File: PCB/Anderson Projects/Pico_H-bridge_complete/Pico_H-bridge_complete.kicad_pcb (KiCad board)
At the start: 2 copper layers, 120.2 x 65.5 mm, 92 parts, among them J1 Screw_Terminal_01x10, J2 Motor Connector, Q1 AO3400A, Q2 AO3400A, Q3 DMP3130LQ-7, Q4 DMP3130LQ-7, SW1 SW_DIP_x01, U1 Pico, U10 SN74LVC1G14DBV, U11 SN74LVC1G14DBV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

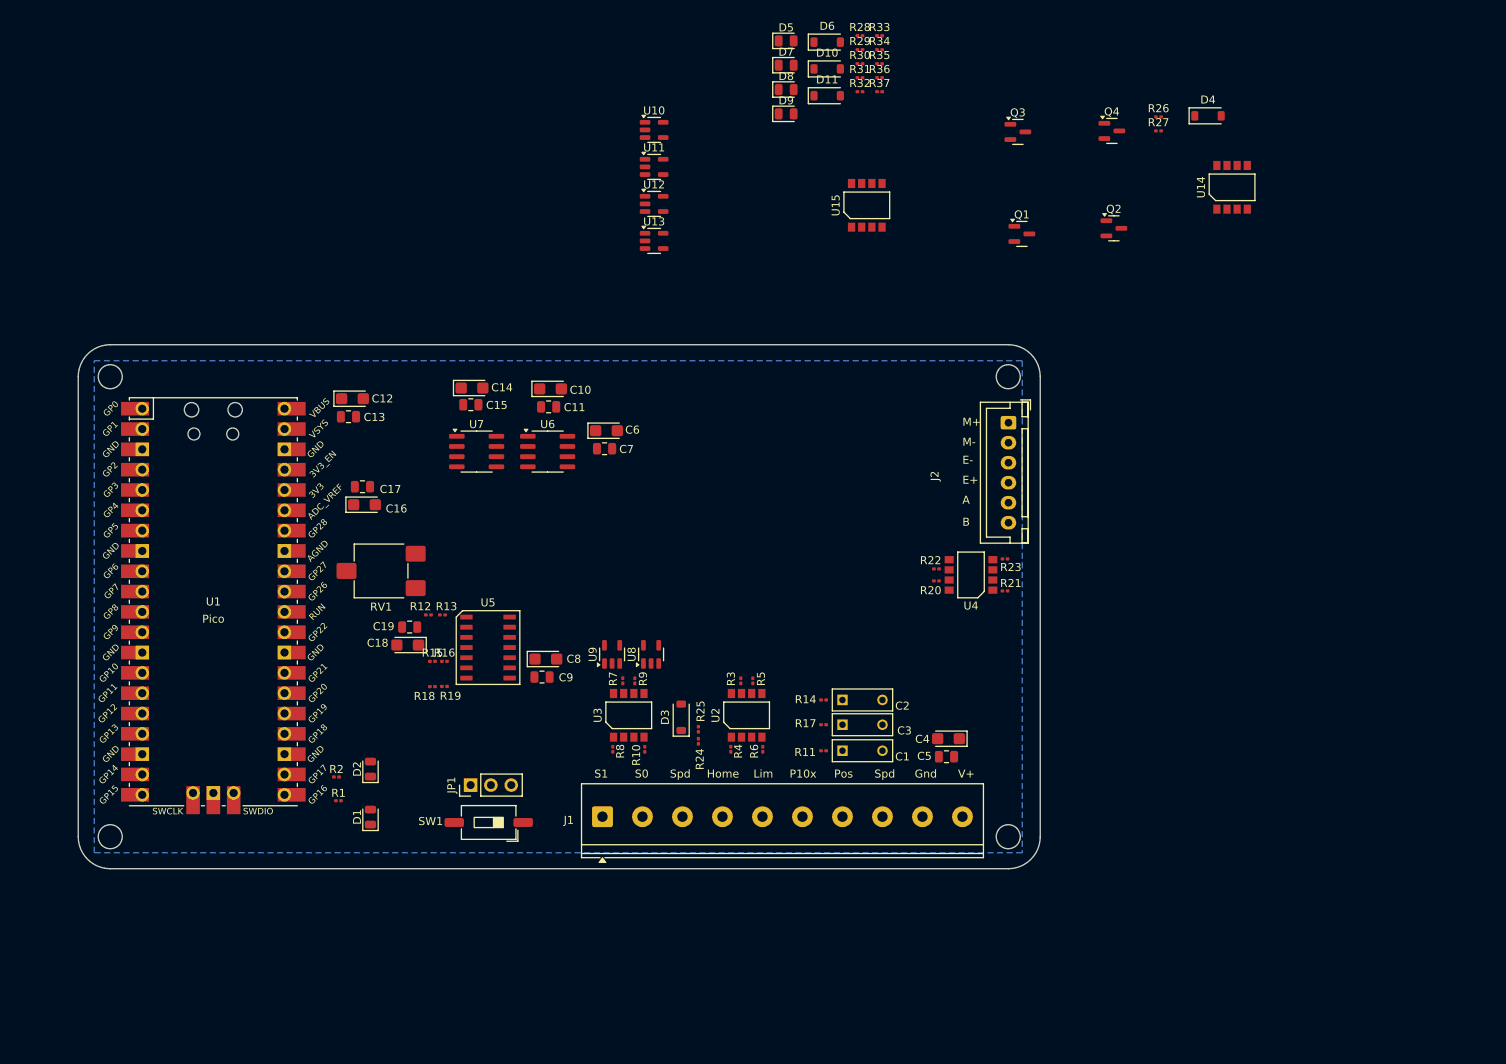
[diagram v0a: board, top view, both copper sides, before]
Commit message: Anderson PCB ready for board layout
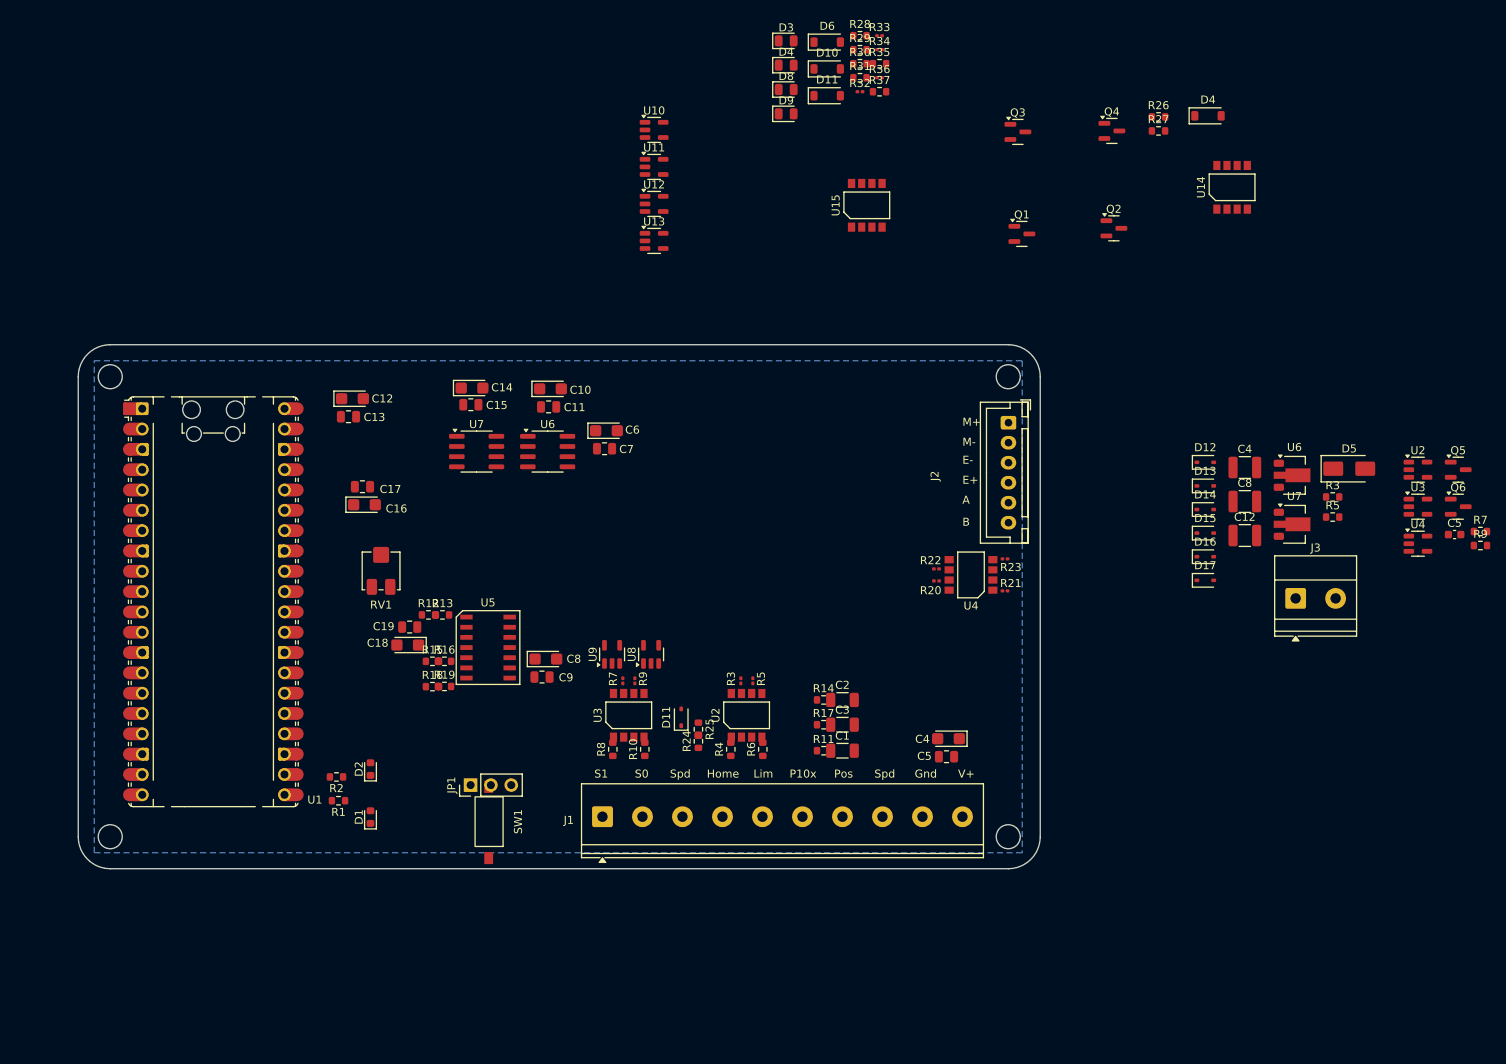
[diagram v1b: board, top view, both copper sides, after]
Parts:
- added C12: 100uF, Capacitor_SMD:C_1210_3225Metric, F.Cu at (228.8, 78.8)
- added C4: 100uF, Capacitor_SMD:C_1210_3225Metric, F.Cu at (228.8, 70.3)
- added C5: 680pF, Capacitor_SMD:C_0603_1608Metric, F.Cu at (255.0, 78.7)
- added C8: 100uF, Capacitor_SMD:C_1210_3225Metric, F.Cu at (228.8, 74.6)
- added D12: 3.3v, Diode_SMD:D_SOD-323, F.Cu at (223.9, 69.7)
- added D13: 3.3v, Diode_SMD:D_SOD-323, F.Cu at (223.9, 72.7)
- added D14: 3.3v, Diode_SMD:D_SOD-323, F.Cu at (223.9, 75.6)
- added D15: 3.3v, Diode_SMD:D_SOD-323, F.Cu at (223.9, 78.5)
- added D16: 3.3v, Diode_SMD:D_SOD-323, F.Cu at (223.9, 81.5)
- added D17: 3.3v, Diode_SMD:D_SOD-323, F.Cu at (223.9, 84.5)
- added D5: D, Diode_SMD:D_SMA, F.Cu at (241.9, 70.5)
- added J3: Screw_Terminal_01x02, TerminalBlock_Phoenix:TerminalBlock_Phoenix_MKDS-1,5-2_1x02_P5.00mm_Horizontal, F.Cu at (235.2, 86.7)
- added Q5: MMBT3904, Package_TO_SOT_SMD:SOT-23, F.Cu at (255.5, 70.6)
- added Q6: MMBT3904, Package_TO_SOT_SMD:SOT-23, F.Cu at (255.5, 75.2)
- added R3: 10k, Resistor_SMD:R_0603_1608Metric, F.Cu at (239.8, 74.0)
- added R5: 10k, Resistor_SMD:R_0603_1608Metric, F.Cu at (239.8, 76.5)
- added R7: 1k, Resistor_SMD:R_0603_1608Metric, F.Cu at (258.3, 78.3)
- added R9: 1k, Resistor_SMD:R_0603_1608Metric, F.Cu at (258.3, 80.1)
- added U2: 74LVC1G08GV, Package_TO_SOT_SMD:SOT-23-5, F.Cu at (250.5, 70.6)
- added U3: 74LVC1G08GV, Package_TO_SOT_SMD:SOT-23-5, F.Cu at (250.5, 75.2)
- added U4: 74LVC1G08GV, Package_TO_SOT_SMD:SOT-23-5, F.Cu at (250.5, 79.9)
- added U6: LM7810, Package_TO_SOT_SMD:SOT-89-3, F.Cu at (235.0, 71.3)
- added U7: LM78L05, Package_TO_SOT_SMD:SOT-89-3, F.Cu at (235.0, 77.5)
- C1, C2, C3: footprint TJR:C_Rect_L7.3mm_W4.5_H9.5mm_P5.0mmx -> Capacitor_SMD:C_1206_3216Metric
- D1, D2: footprint LED_SMD:LED_0805_2012Metric -> LED_SMD:LED_0603_1608Metric
- D11: renamed from D3; value 3.6V -> 3.3v; footprint Diode_SMD:D_SOD-123 -> Diode_SMD:D_SOD-323
- R1, R2: value 330 -> 330Ω; footprint Resistor_SMD:R_0201_0603Metric -> Resistor_SMD:R_0603_1608Metric
- R10, R4, R6, R8: value 4.7k -> 10k; footprint Resistor_SMD:R_0201_0603Metric -> Resistor_SMD:R_0603_1608Metric
- R11, R12, R13, R14, R15, R16, R17, R18, R19, R24, R25: footprint Resistor_SMD:R_0201_0603Metric -> Resistor_SMD:R_0603_1608Metric
- R26, R29: value 470kΩ -> 10k; footprint Resistor_SMD:R_0201_0603Metric -> Resistor_SMD:R_0603_1608Metric
- R27: value 820kΩ -> 110kΩ; footprint Resistor_SMD:R_0201_0603Metric -> Resistor_SMD:R_0603_1608Metric
- R28: value 330Ω -> 2.2kΩ; footprint Resistor_SMD:R_0201_0603Metric -> Resistor_SMD:R_0603_1608Metric
- R30: value 820kΩ -> 2.2kΩ; footprint Resistor_SMD:R_0201_0603Metric -> Resistor_SMD:R_0603_1608Metric
- R31: value 330Ω -> 110kΩ; footprint Resistor_SMD:R_0201_0603Metric -> Resistor_SMD:R_0603_1608Metric
- R35, R37: value 820kΩ -> 10k; footprint Resistor_SMD:R_0201_0603Metric -> Resistor_SMD:R_0603_1608Metric
- RV1: footprint Potentiometer_SMD:Potentiometer_ACP_CA6-VSMD_Vertical -> Potentiometer_SMD:Potentiometer_Bourns_3314J_Vertical
- SW1: footprint Button_Switch_SMD:SW_DIP_SPSTx01_Slide_6.7x4.1mm_W8.61mm_P2.54mm_LowProfile -> CustomBPA:DIP_1x01_3.5_6.2mm
- U1: footprint TJR:RPi_Pico_SMD_TH -> Module:RaspberryPi_Pico_Common_Unspecified
- renumbered D5 to D3, D7 to D4
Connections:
- net Speed PWM renamed Speed_set PWM
- net Speed Set renamed Net-(J1-Pin_3)
- D11 pad 1: Net-(D3-K) -> Speed_set
- D3 pad 1: Net-(D5-K) -> Net-(D3-K)
- D3 pad 2: +5V -> M+
- D4 pad 1: Net-(D7-K) -> Net-(D4-K)
- D4 pad 2: +5V -> M-
- J1 pad 10: +Vsup -> Net-(D5-A)
- Q1 pad 1: Net-(D10-K) -> /H-Bridge/CCW1
- Q2 pad 1: Net-(D11-K) -> /H-Bridge/CW1
- Q2 pad 2: M- -> GND
- Q2 pad 3: GND -> M-
- Q3 pad 1: Net-(D6-A) -> Net-(Q3-G)
- Q3 pad 2: M+ -> +Vsup
- Q3 pad 3: +Vsup -> M+
- Q4 pad 1: Net-(D4-A) -> Net-(Q4-G)
- R10 pad 2: Net-(R10-Pad2) -> S0
- R24 pad 2: Net-(D3-K) -> Speed_set
- R25 pad 1: GND -> Speed_set
- R25 pad 2: Net-(D3-K) -> GND
- R26 pad 1: +Vsup -> Net-(Q4-G)
- R26 pad 2: Net-(D4-A) -> Net-(Q6-C)
- R27 pad 1: Net-(D4-A) -> Net-(Q6-B)
- R27 pad 2: Net-(R27-Pad2) -> /H-Bridge/CCW0
- R28 pad 1: Net-(R28-Pad1) -> +Vsup
- R28 pad 2: Net-(D5-K) -> Net-(Q4-G)
- R29 pad 1: +Vsup -> Net-(Q5-C)
- R29 pad 2: Net-(D6-A) -> Net-(Q3-G)
- R30 pad 1: Net-(D6-A) -> Net-(Q3-G)
- R30 pad 2: Net-(R30-Pad2) -> +Vsup
- R31 pad 1: Net-(D7-K) -> /H-Bridge/CW0
- R31 pad 2: Net-(R31-Pad2) -> Net-(Q5-B)
- R35 pad 1: Net-(D10-K) -> /H-Bridge/CCW1
- R37 pad 1: Net-(D11-K) -> /H-Bridge/CW1
- R4 pad 2: Net-(R4-Pad2) -> Home
- R6 pad 2: Net-(R6-Pad2) -> Limit Switch
- R8 pad 2: Net-(R8-Pad2) -> S1
- U1 pad 12: GND -> unconnected-(U1-GPIO9-Pad12)
- U1 pad 13: unconnected-(U1-GND-Pad13)_1 -> GND
- U1 pad 28: unconnected-(U1-GND-Pad28) -> GND
- U1 pad 31: Net-(D3-K) -> Speed_set
- U1 pad 33: unconnected-(U1-AGND-Pad33) -> GND
- U1 pad 35: unconnected-(U1-ADC_VREF-Pad35) -> +3.3V
- U10 pad 4: /H-Bridge/CW1 -> Net-(U10-Pad4)
- U12 pad 1: /H-Bridge/CCW1 -> Net-(U10-Pad2)
- U12 pad 2: Net-(U10-Pad2) -> Net-(U12-Pad2)
- U12 pad 4: /H-Bridge/CCW0 -> /H-Bridge/CCW1
- U13 pad 1: Net-(U11-Pad2) -> Net-(U13-Pad1)
- U13 pad 2: /H-Bridge/CW1 -> Net-(U10-Pad2)
- U13 pad 4: /H-Bridge/CW0 -> /H-Bridge/CW1
- U8 pad 4: Net-(U11-Pad2) -> Net-(U13-Pad1)
- U9 pad 4: Net-(U10-Pad2) -> Net-(U12-Pad2)

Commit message: Anderson Pico_H-bridge_complete Gerbers ready to order
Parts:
- removed C10, C14, C16, C18, C6: 100uF, Capacitor_Tantalum_SMD:CP_EIA-3216-10_Kemet-I
- removed C11, C13, C15, C17, C19, C7, C9: 0.1uF, Capacitor_SMD:C_0805_2012Metric
- removed the C12 at (117.3, 61.8)
- removed the C4 at (191.8, 104.2)
- removed the C5 at (191.5, 106.5)
- removed the C8 at (141.5, 94.3)
- removed D10, D6: 4.9v, Diode_SMD:D_SOD-123
- removed the D11 at (176.6, 23.9)
- removed the D4 at (171.5, 20.1)
- removed D8, D9: LED, LED_SMD:LED_0805_2012Metric
- removed the G*** at (99.7, 98.4)
- removed R20, R22: 10k, Resistor_SMD:R_0201_0603Metric
- removed R21, R23: 4.7k, Resistor_SMD:R_0201_0603Metric
- removed the R3 at (165.8, 97.0)
- removed R32, R33: 330Ω, Resistor_SMD:R_0201_0603Metric
- removed R34, R36: 470kΩ, Resistor_SMD:R_0201_0603Metric
- removed the R5 at (167.3, 97.0)
- removed the R7 at (151.1, 97.0)
- removed the R9 at (152.6, 97.0)
- removed U11: SN74LVC1G14DBV, Package_TO_SOT_SMD:SOT-23-5
- removed U14, U15: ILD217T, CustomBPA:SOIC-8_5.46mm_P1.27
- removed the U2 at (250.5, 70.6)
- removed the U3 at (250.5, 75.2)
- removed the U4 at (250.5, 79.9)
- removed the U6 at (235.0, 71.3)
- removed the U7 at (235.0, 77.5)
- added G***: LOGO, CustomBPA:Bengal_25_25, F.Cu at (150.9, 79.6)
- added G***: LOGO, CustomBPA:Bengal_50_50, B.Cu at (148.6, 87.1)
- added TP1: Spd(0-3.3), TestPoint:TestPoint_Loop_D2.50mm_Drill1.0mm, F.Cu at (134.6, 59.3)
- added TP10: CW0, TestPoint:TestPoint_Loop_D2.50mm_Drill1.0mm, F.Cu at (138.9, 59.3)
- added TP11: CCW1, TestPoint:TestPoint_Loop_D2.50mm_Drill1.0mm, F.Cu at (147.6, 59.3)
- added TP2: 10v, TestPoint:TestPoint_Loop_D2.50mm_Drill1.0mm, F.Cu at (173.6, 59.3)
- added TP3: 5v, TestPoint:TestPoint_Loop_D2.50mm_Drill1.0mm, F.Cu at (177.9, 59.3)
- added TP4: S0, TestPoint:TestPoint_Loop_D2.50mm_Drill1.0mm, F.Cu at (156.2, 59.3)
- added TP5: S1, TestPoint:TestPoint_Loop_D2.50mm_Drill1.0mm, F.Cu at (160.6, 59.3)
- added TP6: Q3, TestPoint:TestPoint_Loop_D2.50mm_Drill1.0mm, F.Cu at (164.9, 59.3)
- added TP7: Q4, TestPoint:TestPoint_Loop_D2.50mm_Drill1.0mm, F.Cu at (169.2, 59.3)
- added TP8: CCW0, TestPoint:TestPoint_Loop_D2.50mm_Drill1.0mm, F.Cu at (151.9, 59.3)
- added TP9: CW1, TestPoint:TestPoint_Loop_D2.50mm_Drill1.0mm, F.Cu at (143.2, 59.3)
- D4: value 4.9v -> LED; footprint Diode_SMD:D_SOD-123 -> LED_SMD:LED_0805_2012Metric
- U1: footprint Module:RaspberryPi_Pico_Common_Unspecified -> CustomBPA:RaspberryPi_Pico
- U2, U3, U4: value ILD217T -> 74LVC1G08GV; footprint CustomBPA:SOIC-8_5.46mm_P1.27 -> Package_TO_SOT_SMD:SOT-23-5
- U6: footprint Package_SO:SOIC-8_3.9x4.9mm_P1.27mm -> Package_TO_SOT_SMD:SOT-89-3
- U7: value LM78L05_SO8 -> LM78L05; footprint Package_SO:SOIC-8_3.9x4.9mm_P1.27mm -> Package_TO_SOT_SMD:SOT-89-3
- moved Q5 116.8 mm to (138.7, 72.7), turned to 180 degrees
- moved R7 109.6 mm to (148.8, 74.3), turned to 180 degrees
- moved R9 106.3 mm to (152.0, 78.1)
- moved D15 98.3 mm to (129.5, 106.1), turned to -90 degrees
- moved D14 94.2 mm to (134.7, 106.1), turned to -90 degrees
- moved Q6 92.7 mm to (162.8, 73.0)
- moved D4 86.7 mm to (152.0, 74.3)
- moved D13 86.5 mm to (143.8, 105.4)
- moved D12 83.2 mm to (148.8, 105.4)
- moved C5 78.8 mm to (176.2, 80.9), turned to -90 degrees
- moved D5 74.7 mm to (178.6, 110.1), turned to -90 degrees
- moved R35 74.3 mm to (142.9, 82.3), turned to -90 degrees
- moved U10 72.9 mm to (154.1, 101.0), turned to 180 degrees
- moved Q4 70.9 mm to (155.2, 70.4), turned to 180 degrees
- moved Q2 70.9 mm to (155.2, 82.2), turned to 180 degrees
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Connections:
- D4 pad 1: +Vsup -> Net-(D4-K)
- D4 pad 2: Net-(D4-A) -> M-
- J3 pad 1: M+ -> M-
- J3 pad 2: M- -> M+
- U2 pad 1: Net-(R4-Pad2) -> Net-(U13-Pad1)
- U2 pad 2: GND_PLC -> Net-(U10-Pad4)
- U2 pad 3: GND_PLC -> GND
- U2 pad 4: Net-(R6-Pad2) -> /H-Bridge/CW0
- U2 pad 5: GND -> +5V
- U3 pad 1: Net-(R8-Pad2) -> Net-(U10-Pad4)
- U3 pad 2: GND_PLC -> Net-(U12-Pad2)
- U3 pad 3: GND_PLC -> GND
- U3 pad 4: Net-(R10-Pad2) -> /H-Bridge/CCW0
- U3 pad 5: GND -> +5V
- U4 pad 1: Net-(R21-Pad2) -> Net-(U13-Pad1)
- U4 pad 2: GND -> Net-(U12-Pad2)
- U4 pad 4: Net-(R23-Pad2) -> Net-(U10-Pad2)
- U4 pad 5: GND -> +5V
- U6 pad 3: GND -> +Vsup
- U7 pad 3: GND -> +10V
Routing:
- net +10V: track 0.00 -> 133.2 mm, vias 0 -> 2
- net S1: track 0.00 -> 101.1 mm, vias 0 -> 3
- net S0: track 0.00 -> 99.4 mm, vias 0 -> 3
- net A: track 0.00 -> 99.1 mm, vias 0 -> 2
- net B: track 0.00 -> 97.8 mm, vias 0 -> 2
- net +Vsup: track 0.00 -> 92.6 mm, vias 0 -> 3
- net /H-Bridge/CW1: track 0.00 -> 83.3 mm, vias 0 -> 3
- net Speed_set: track 0.00 -> 82.5 mm, vias 0 -> 1
- net Limit Switch: track 0.00 -> 73.9 mm
- net Net-(JP1-C): track 0.00 -> 72.6 mm, vias 0 -> 1
- net M+: track 0.00 -> 71.7 mm
- net /H-Bridge/CCW0: track 0.00 -> 61.6 mm, vias 0 -> 3
- net M-: track 0.00 -> 60.0 mm
- net Home: track 0.00 -> 59.2 mm
- net Analog Position x10: track 0.00 -> 57.7 mm, vias 0 -> 1
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- added copper zone on In1.Cu, net +3.3V
- added copper zone on In1.Cu, net +5V
- added copper zone on F.Cu, net GND
- added copper zone on In2.Cu, net GND
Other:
- board size 120.2 x 65.5 mm -> 103.4 x 65.5 mm
- copper layers 2 -> 4
- board text added: "Fwd"
- board text added: "Max Speed Cal"
- board text added: "Modes PWM Simple"
- board text added: "Motor Select"
- board text added: "PLC Motor Interface Board Anderson - rev0 June 2025"
- board text added: "Rev"
- board text added: "S0 S1 0 0 : Coast 0 1 : CW 1 0 : CCW 1 1 : Brake"
